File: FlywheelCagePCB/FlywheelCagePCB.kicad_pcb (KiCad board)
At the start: 2 copper layers, 47.9 x 24.8 mm, 6 parts, among them J1 Conn_01x05, J2 Conn_01x05, Q1 SFH320, U1 QRE1113GR, U2 SN74LVC2G14DBV, U3 SPX3819M5-L-3-3

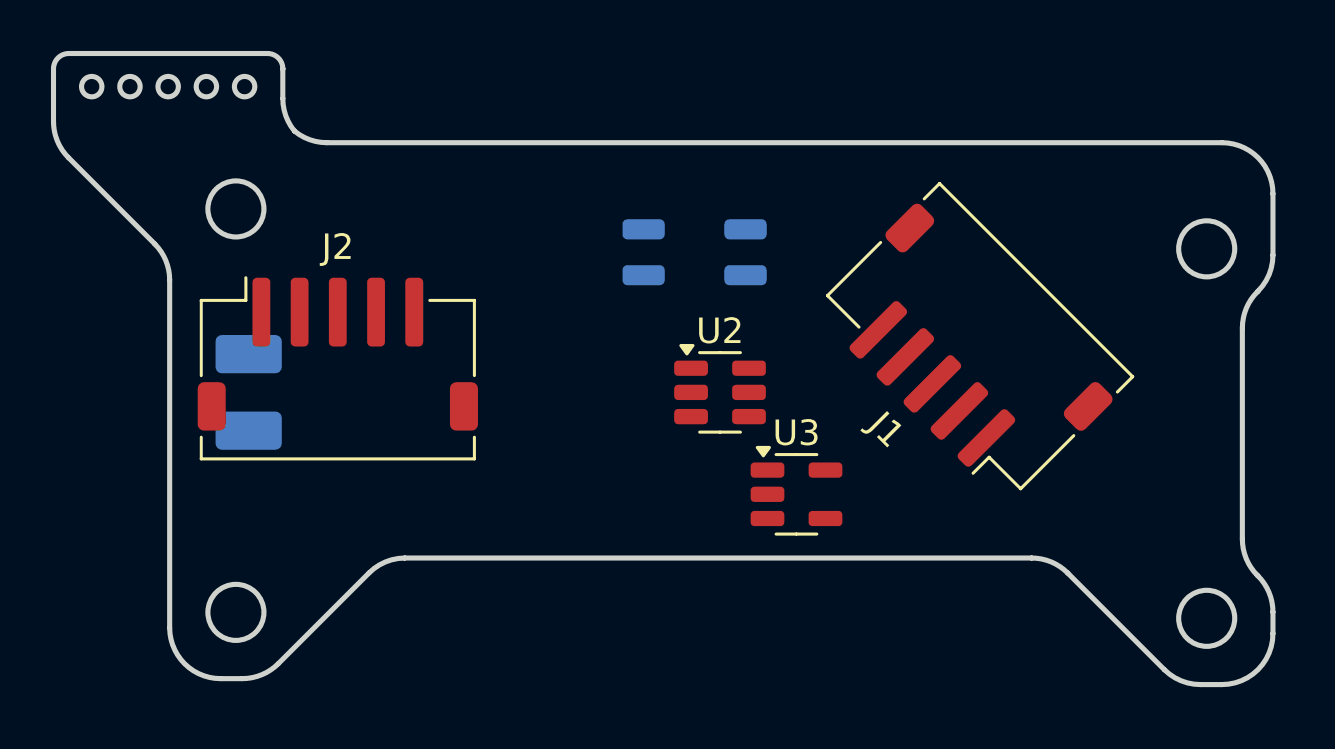
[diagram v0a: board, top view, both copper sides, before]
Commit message: added resistors to flywheel pcb
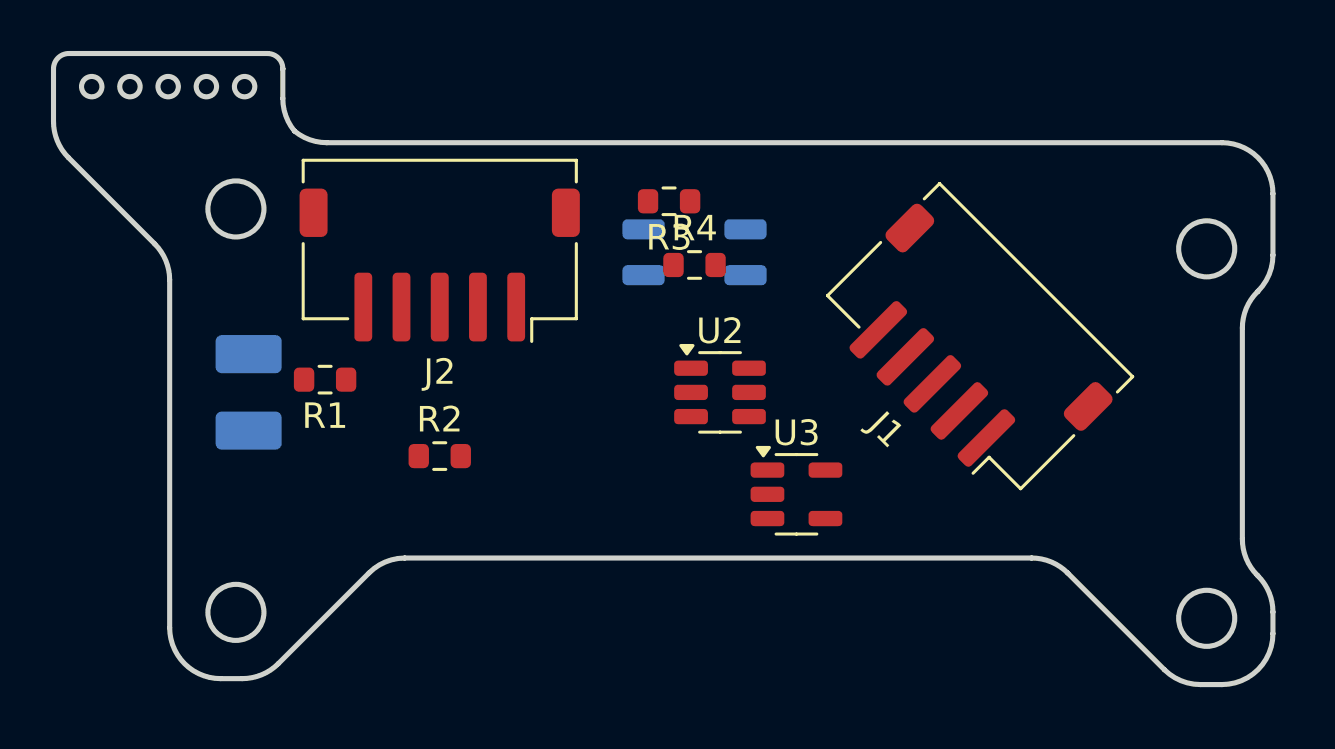
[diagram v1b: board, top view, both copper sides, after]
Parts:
- added R1: 3.3k, Resistor_SMD:R_0603_1608Metric, F.Cu at (83.0, 98.0)
- added R2: 220, Resistor_SMD:R_0603_1608Metric, F.Cu at (87.5, 101.0)
- added R3: 470, Resistor_SMD:R_0603_1608Metric, F.Cu at (96.5, 91.0)
- added R4: 15.0K, Resistor_SMD:R_0603_1608Metric, F.Cu at (97.5, 93.5)
- moved J2 5.32 mm to (87.5, 93.5), turned to 180 degrees
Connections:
- net /temp renamed temp2
- net Net-(J1-Pin_3) renamed /tach_d
- net Net-(J1-Pin_4) renamed /breakbeam_d
- net Net-(Q1-C) renamed /breakbeam_a
- net Net-(U2-2A) renamed /tach_a

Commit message: moved PCB components a bit
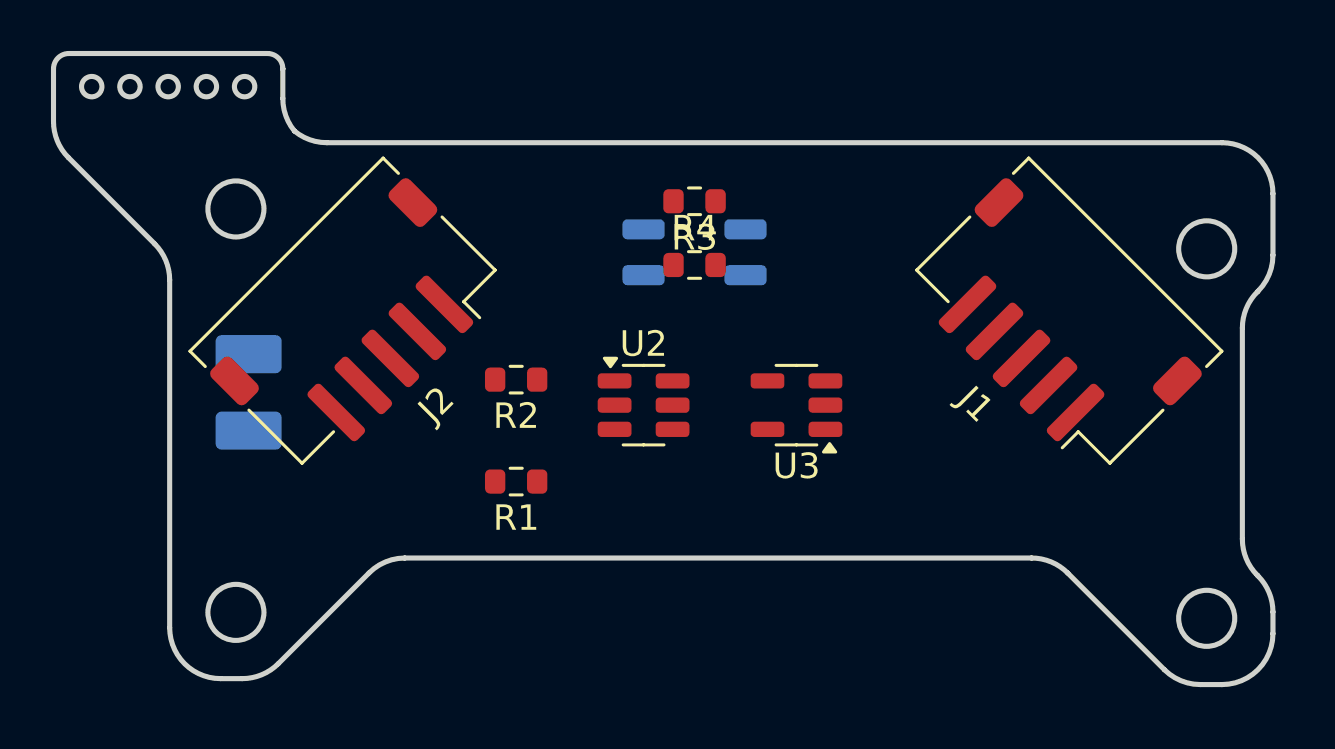
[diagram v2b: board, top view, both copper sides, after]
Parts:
- moved R1 8.50 mm to (90.5, 102.0)
- moved R2 4.24 mm to (90.5, 98.0), turned to 180 degrees
- moved J2 3.99 mm to (84.4, 96.0), turned to -135 degrees
- moved J1 3.64 mm to (111.5, 96.0)
- moved U3 3.50 mm to (101.5, 99.0), turned to 180 degrees
- moved U2 3.04 mm to (95.5, 99.0)
- moved R3 1.00 mm to (97.5, 91.0)

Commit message: Added 3d models for JST ZH connectors.  Made 3d Step output
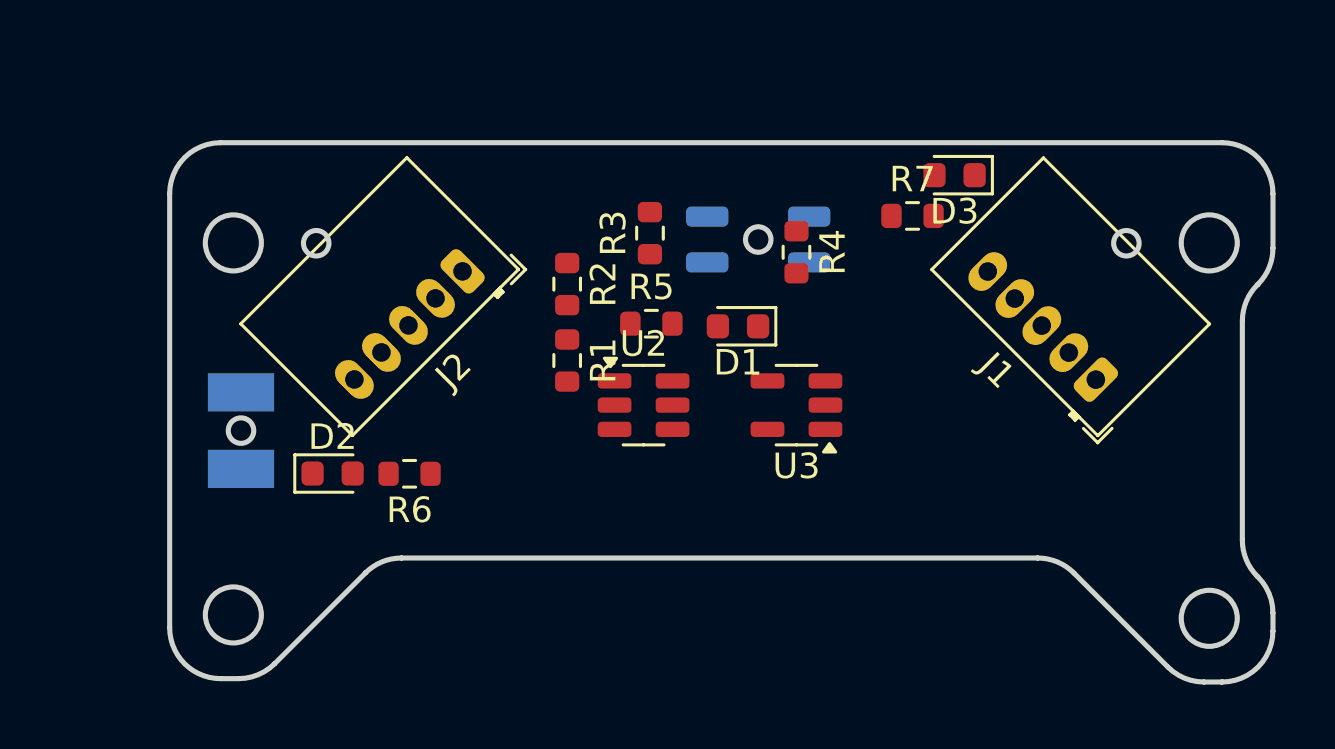
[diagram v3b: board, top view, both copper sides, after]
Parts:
- removed Q1: SFH320, LED_SMD:LED_PLCC-2_3.4x3.0mm_KA
- added D1: Red, LED_SMD:LED_0603_1608Metric, F.Cu at (99.2, 95.9)
- added D2: Red, LED_SMD:LED_0603_1608Metric, F.Cu at (83.3, 101.7)
- added D3: Green, LED_SMD:LED_0603_1608Metric, F.Cu at (107.7, 90.0)
- added D4: SFH_320-4-Z, McLibrary:PHODET_SFH_320-4-Z, B.Cu at (79.7, 100.0)
- added R5: 330, Resistor_SMD:R_0603_1608Metric, F.Cu at (95.8, 95.8)
- added R6: 330, Resistor_SMD:R_0603_1608Metric, F.Cu at (86.3, 101.7)
- added R7: 330, Resistor_SMD:R_0603_1608Metric, F.Cu at (106.1, 91.6)
- J1, J2: footprint Connector_JST:JST_ZH_S5B-ZR-SM4A-TF_1x05-1MP_P1.50mm_Horizontal -> McLibrary:JST_ZH_B5B-ZR_1x05_P1.50mm_Horizontal
- moved R1 5.15 mm to (92.5, 97.2), turned to -90 degrees
- moved J2 4.59 mm to (88.4, 93.8)
- moved R2 4.25 mm to (92.5, 94.2), turned to -90 degrees
- moved R4 4.03 mm to (101.5, 93.0), turned to -90 degrees
- moved J1 2.66 mm to (113.2, 98.0)
- moved U1 2.55 mm to (100.0, 92.5)
- moved R3 2.15 mm to (95.8, 92.2), turned to 90 degrees
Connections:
- net Net-(J2-Pin_2) renamed /breakbeam_led
- net Net-(U1-A) renamed /tach_led
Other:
- board size 47.9 x 24.8 mm -> 43.3 x 21.2 mm

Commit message: Added caps.  Need to get part numbers
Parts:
- added C1: 0.01uf, Capacitor_SMD:C_0603_1608Metric, F.Cu at (100.7, 99.0)
- added C2: 1uf, Capacitor_SMD:C_0603_1608Metric, F.Cu at (101.5, 101.7)
- added C3: 0.1uf, Capacitor_SMD:C_0603_1608Metric, F.Cu at (98.7, 100.0)
- moved U3 2.25 mm to (103.7, 99.0)
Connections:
- U3 pad 4: unconnected-(U3-BP-Pad4) -> Net-(U3-BP)

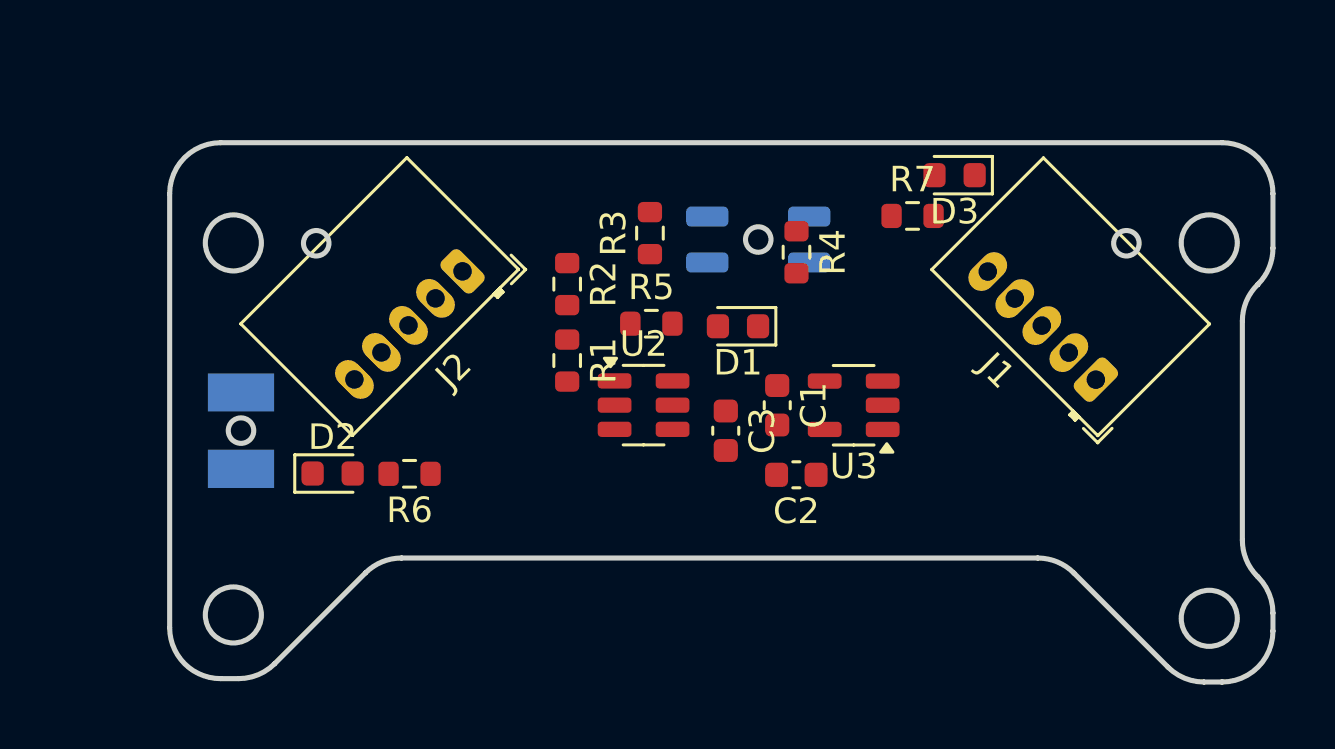
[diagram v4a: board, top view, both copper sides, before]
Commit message: placement complete.  started routing
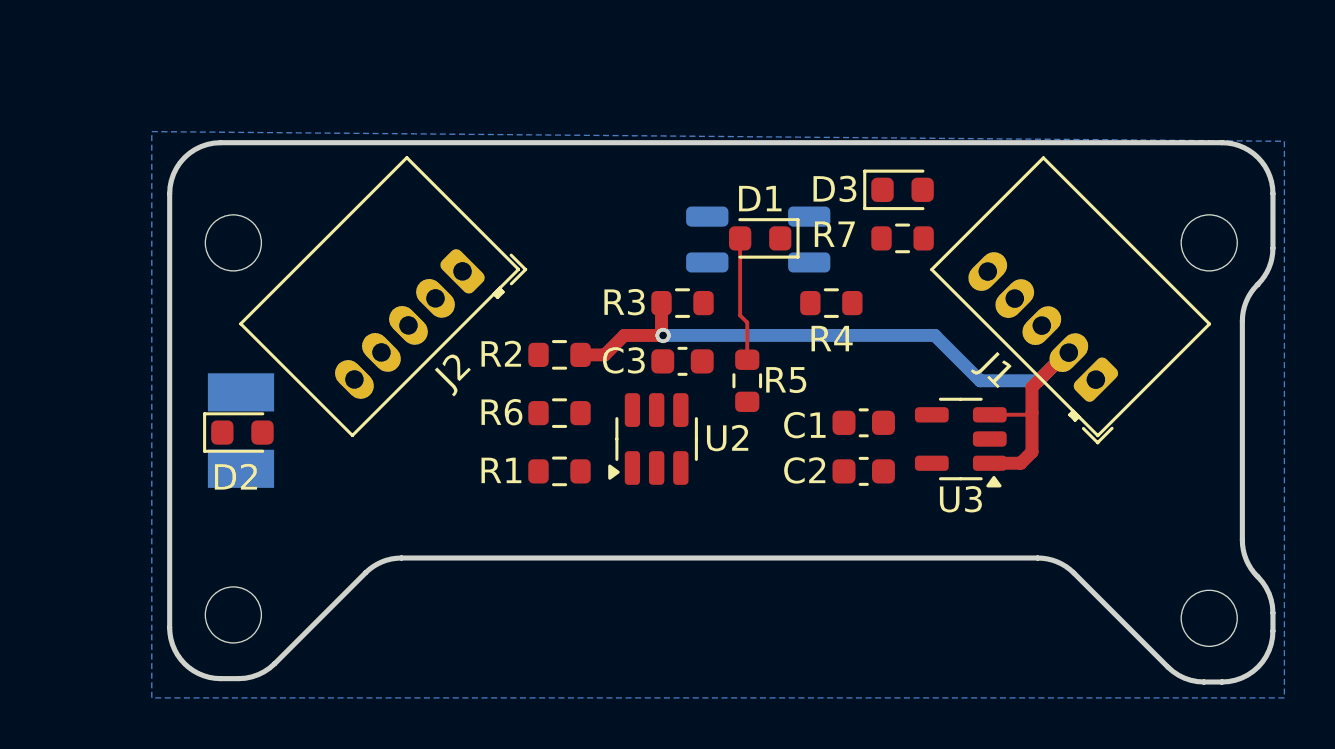
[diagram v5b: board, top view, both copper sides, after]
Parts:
- added REF**: MountingHole_2.2mm_M2, MountingHole:MountingHole_2.2mm_M2, F.Cu at (79.4, 107.2)
- added REF**: MountingHole_2.2mm_M2, MountingHole:MountingHole_2.2mm_M2, F.Cu at (79.4, 92.6)
- added REF**: MountingHole_2.2mm_M2, MountingHole:MountingHole_2.2mm_M2, F.Cu at (117.7, 107.4)
- added REF**: MountingHole_2.2mm_M2, MountingHole:MountingHole_2.2mm_M2, F.Cu at (117.7, 92.6)
- moved R6 6.35 mm to (92.2, 99.3)
- moved U3 4.41 mm to (108.0, 100.3)
- moved R5 4.38 mm to (99.6, 98.0), turned to 90 degrees
- moved R1 4.36 mm to (92.2, 101.6), turned to 0 degrees
- moved D2 3.89 mm to (79.8, 100.1)
- moved D1 3.56 mm to (100.1, 92.5)
- moved C1 3.46 mm to (104.1, 99.7), turned to 180 degrees
- moved C3 3.21 mm to (97.0, 97.3), turned to 0 degrees
- moved R3 3.03 mm to (97.0, 95.0), turned to 0 degrees
- moved R2 2.79 mm to (92.2, 97.0), turned to 180 degrees
- moved C2 2.65 mm to (104.1, 101.6)
- moved R4 2.42 mm to (102.9, 95.0), turned to 180 degrees
- moved D3 2.12 mm to (105.7, 90.6), turned to 0 degrees
- moved U2 1.43 mm to (96.0, 100.3), turned to 90 degrees
- moved R7 0.96 mm to (105.7, 92.5)
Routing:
- net +5V: track 0.00 -> 30.0 mm, vias 0 -> 1
- net /tach_led_ind: track 0.00 -> 4.88 mm
- added copper zone on B.Cu, net GND
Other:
- outline, holes or cut-outs redrawn

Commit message: Tape out on V0.1
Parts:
- moved R5 3.64 mm to (98.8, 94.5), turned to 0 degrees
- moved R3 1.85 mm to (95.2, 94.5), turned to 180 degrees
- moved U2 1.52 mm to (96.0, 101.9)
- moved C3 1.27 mm to (97.0, 98.6)
- moved C2 1.14 mm to (105.2, 102.1), turned to -90 degrees
- moved R1 0.76 mm to (92.2, 102.4)
- moved R2 0.76 mm to (92.2, 96.3)
- moved R6 0.76 mm to (92.2, 100.1)
- moved D3 0.51 mm to (105.2, 90.6)
- moved R4 0.51 mm to (102.9, 94.5)
- moved R7 0.51 mm to (105.2, 92.5)
- moved C1 0.38 mm to (104.1, 99.3)
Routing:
- net +3.3V: track 0.00 -> 41.6 mm, vias 0 -> 5
- net temp2: track 0.00 -> 25.2 mm, vias 0 -> 1
- net /tach_d: track 0.00 -> 23.0 mm, vias 0 -> 3
- net /breakbeam_d: track 0.00 -> 21.8 mm, vias 0 -> 1
- net /breakbeam_a: track 0.00 -> 19.3 mm, vias 0 -> 1
- net /tach_a: track 0.00 -> 13.9 mm, vias 0 -> 2
- net /breakbeam_led_ind: track 0.00 -> 10.8 mm
- net GND: track 0.00 -> 9.89 mm, vias 0 -> 6
- net /tach_led: track 0.00 -> 6.22 mm, vias 0 -> 1
- net /breakbeam_led: track 0.00 -> 4.65 mm
- net /tach_led_ind: track 4.88 -> 2.17 mm
- net Net-(U3-BP): track 0.00 -> 1.92 mm
- net /power_led_ind: track 0.00 -> 1.91 mm
- net +5V: track 30.0 -> 29.9 mm, vias 1 -> 0
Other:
- board text added: "Dart"
- board text added: "Flywheel Cage Sensor Board"
- board text added: "NerfTech"
- board text added: "Pwr"
- board text added: "Tach"

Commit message: BOM scrubb
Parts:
- J1, J2: value Conn_01x05 -> JST_ZH_S5B
